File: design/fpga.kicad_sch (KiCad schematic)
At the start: 83 parts, among them J7 DEBUG_FPGA_GPIO, J8 DIGILENT_JTAG_HS2_01X06, SW1 RST, SW2 PROG, U13 XC7S15-FTGB196, U14 IS25LP064A-JKx

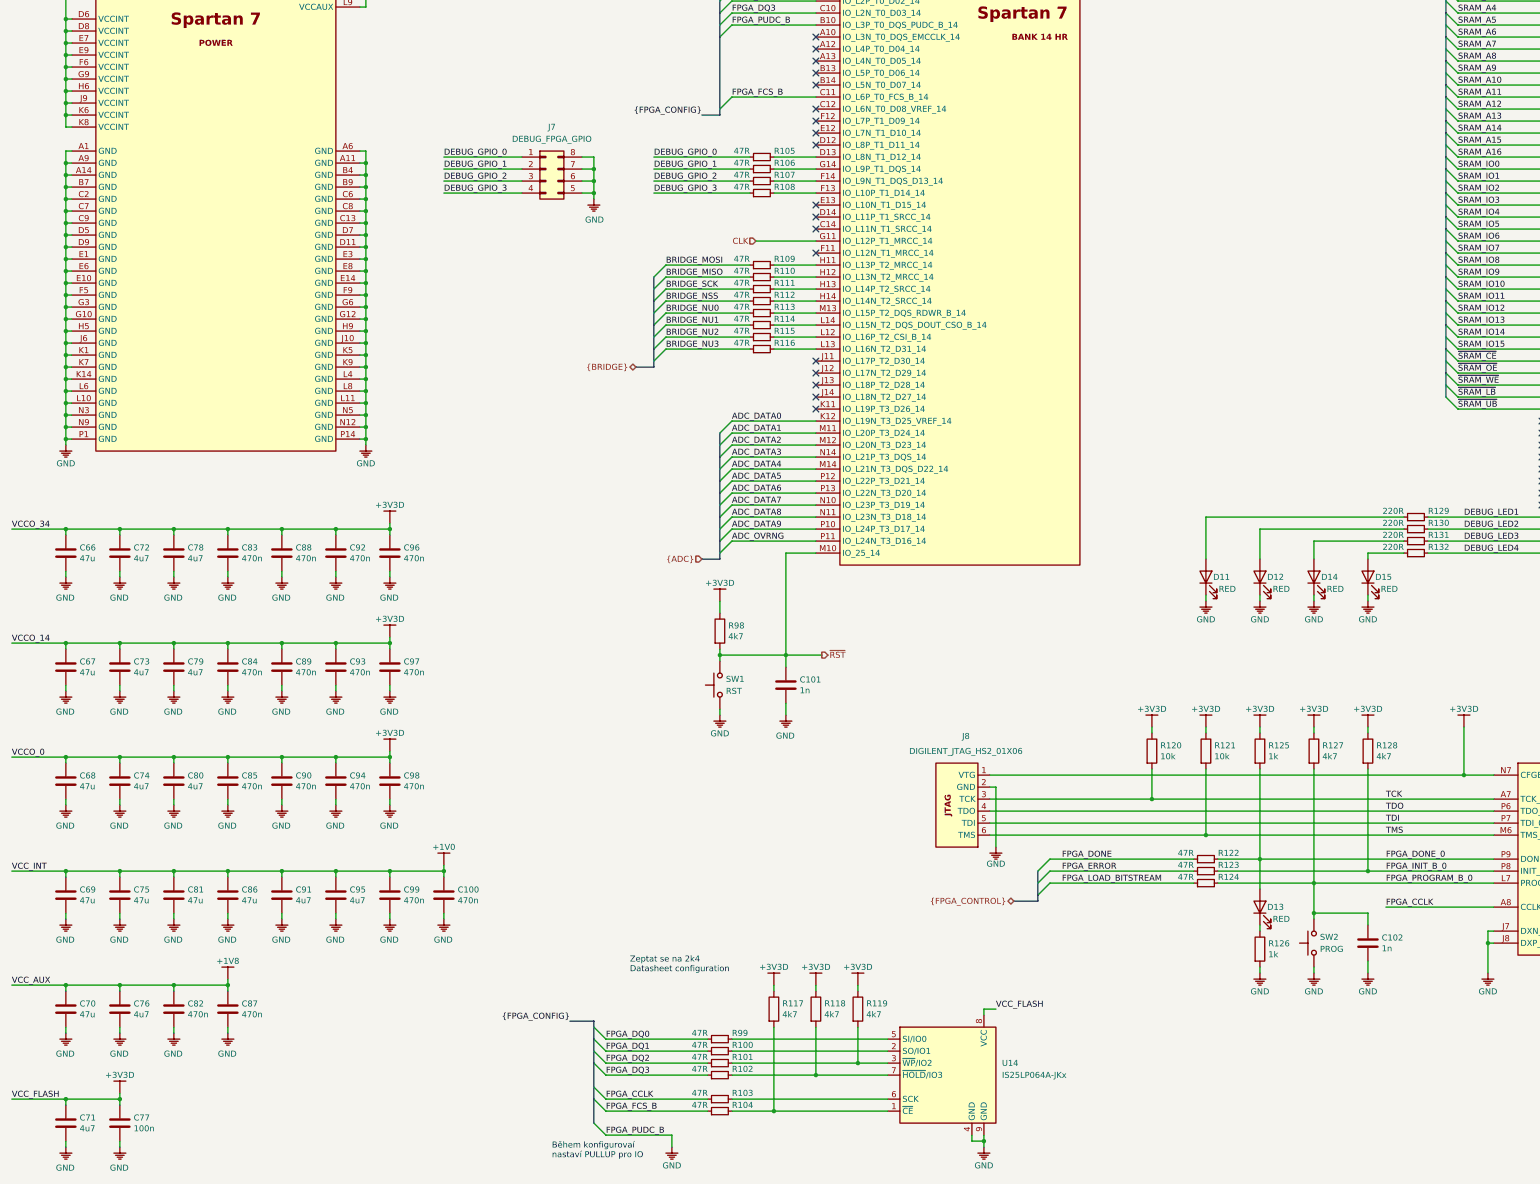
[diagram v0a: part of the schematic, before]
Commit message: Added ADC placement
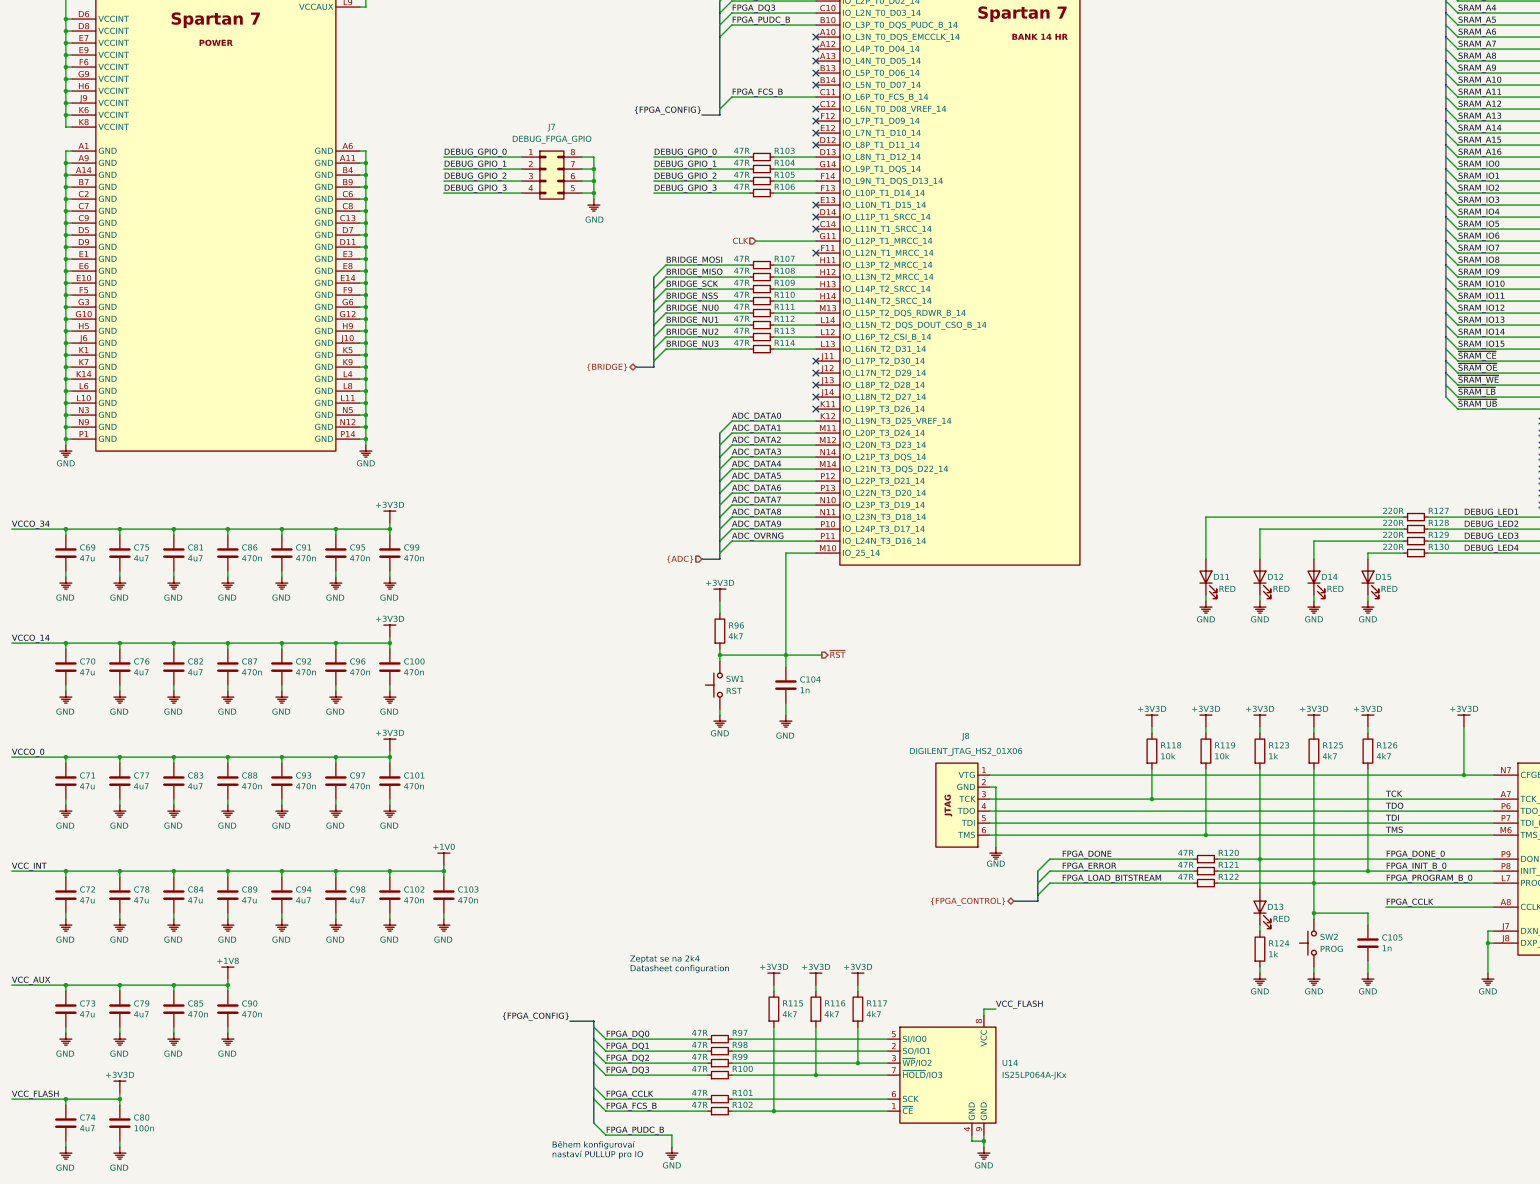
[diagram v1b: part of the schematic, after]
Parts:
- renumbered C97 to C100, C98 to C101, C99 to C102, C100 to C103, C101 to C104, C102 to C105, C66 to C69, C67 to C70, C68 to C71, C69 to C72, C70 to C73, C71 to C74, C72 to C75, C73 to C76, C74 to C77, C75 to C78, C76 to C79, C77 to C80, C78 to C81, C79 to C82, C80 to C83, C81 to C84, C82 to C85, C83 to C86, C84 to C87, C85 to C88, C86 to C89, C87 to C90, C88 to C91, C89 to C92, C90 to C93, C91 to C94, C92 to C95, C93 to C96, C94 to C97, C95 to C98, C96 to C99, R102 to R100, R103 to R101, R104 to R102, R105 to R103, R106 to R104, R107 to R105, R108 to R106, R109 to R107, R110 to R108, R111 to R109, R112 to R110, R113 to R111, R114 to R112, R115 to R113, R116 to R114, R117 to R115, R118 to R116, R119 to R117, R120 to R118, R121 to R119, R122 to R120, R123 to R121, R124 to R122, R125 to R123, R126 to R124, R127 to R125, R128 to R126, R129 to R127, R130 to R128, R131 to R129, R132 to R130, R98 to R96, R99 to R97, R100 to R98, R101 to R99

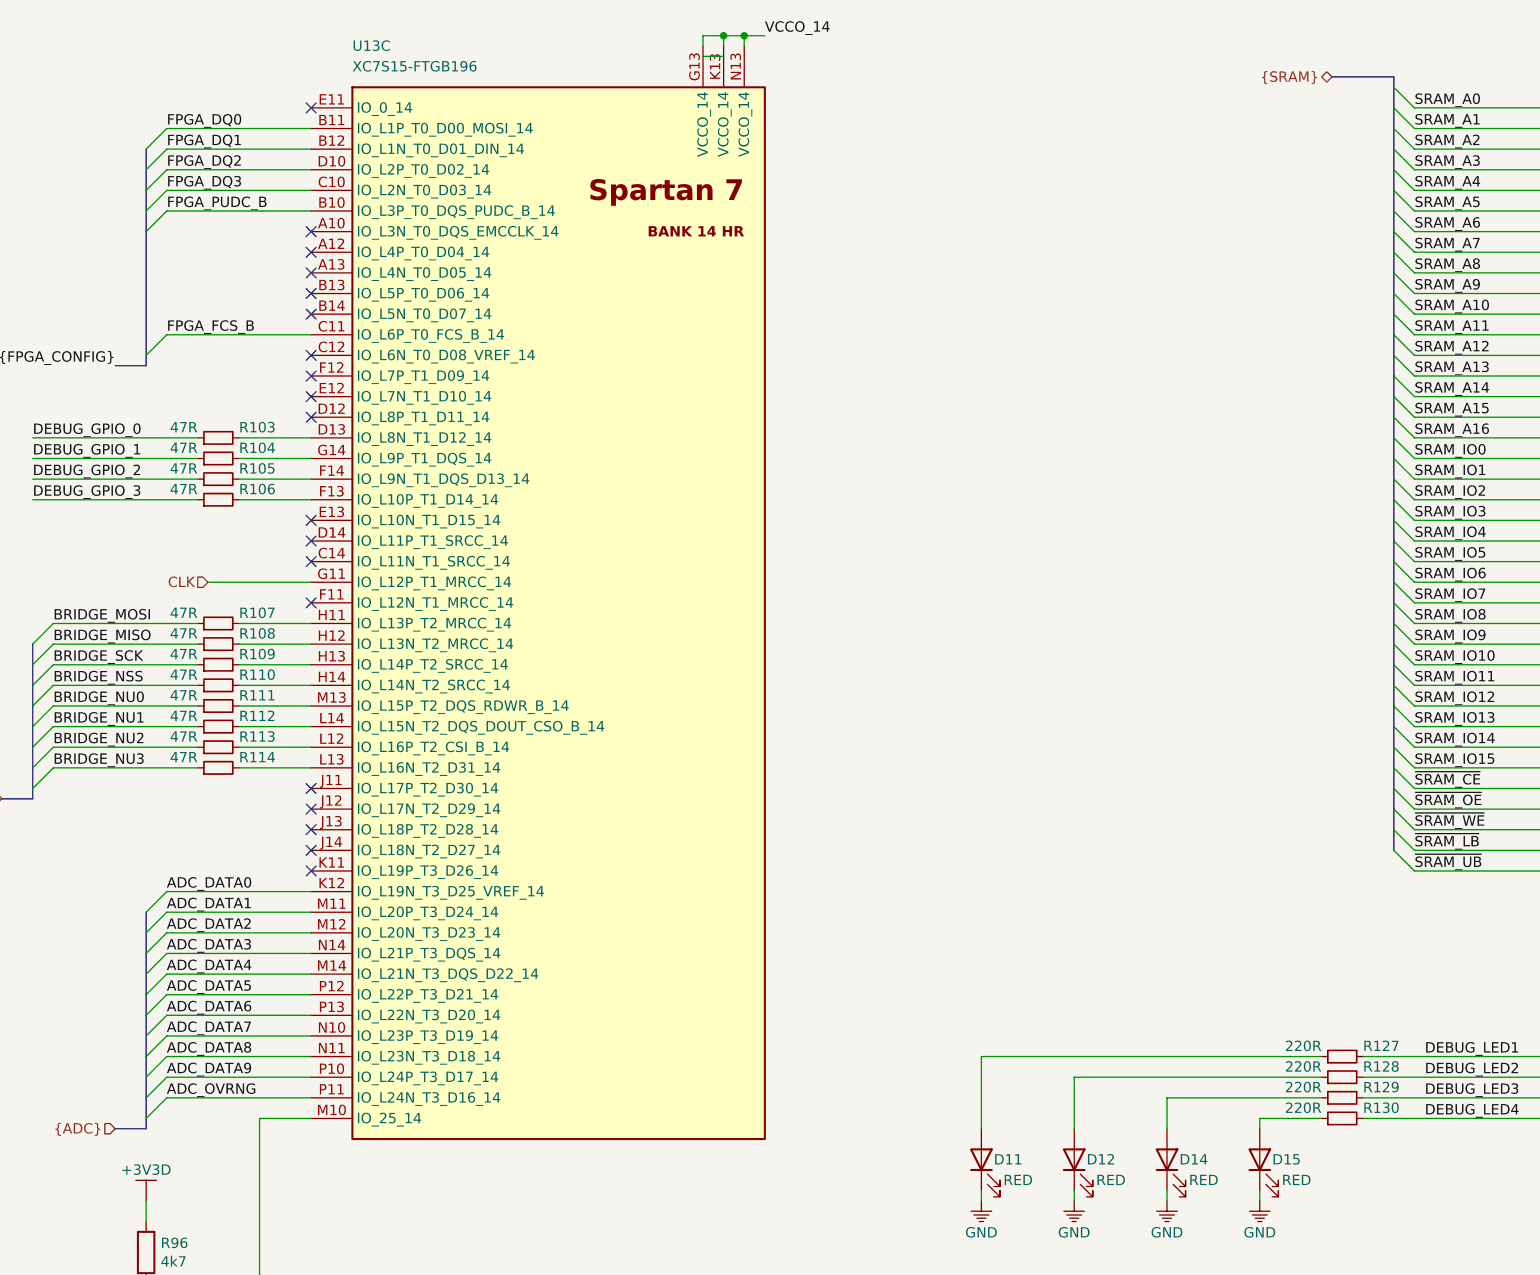
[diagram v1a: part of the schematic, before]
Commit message: Fixed LNA power
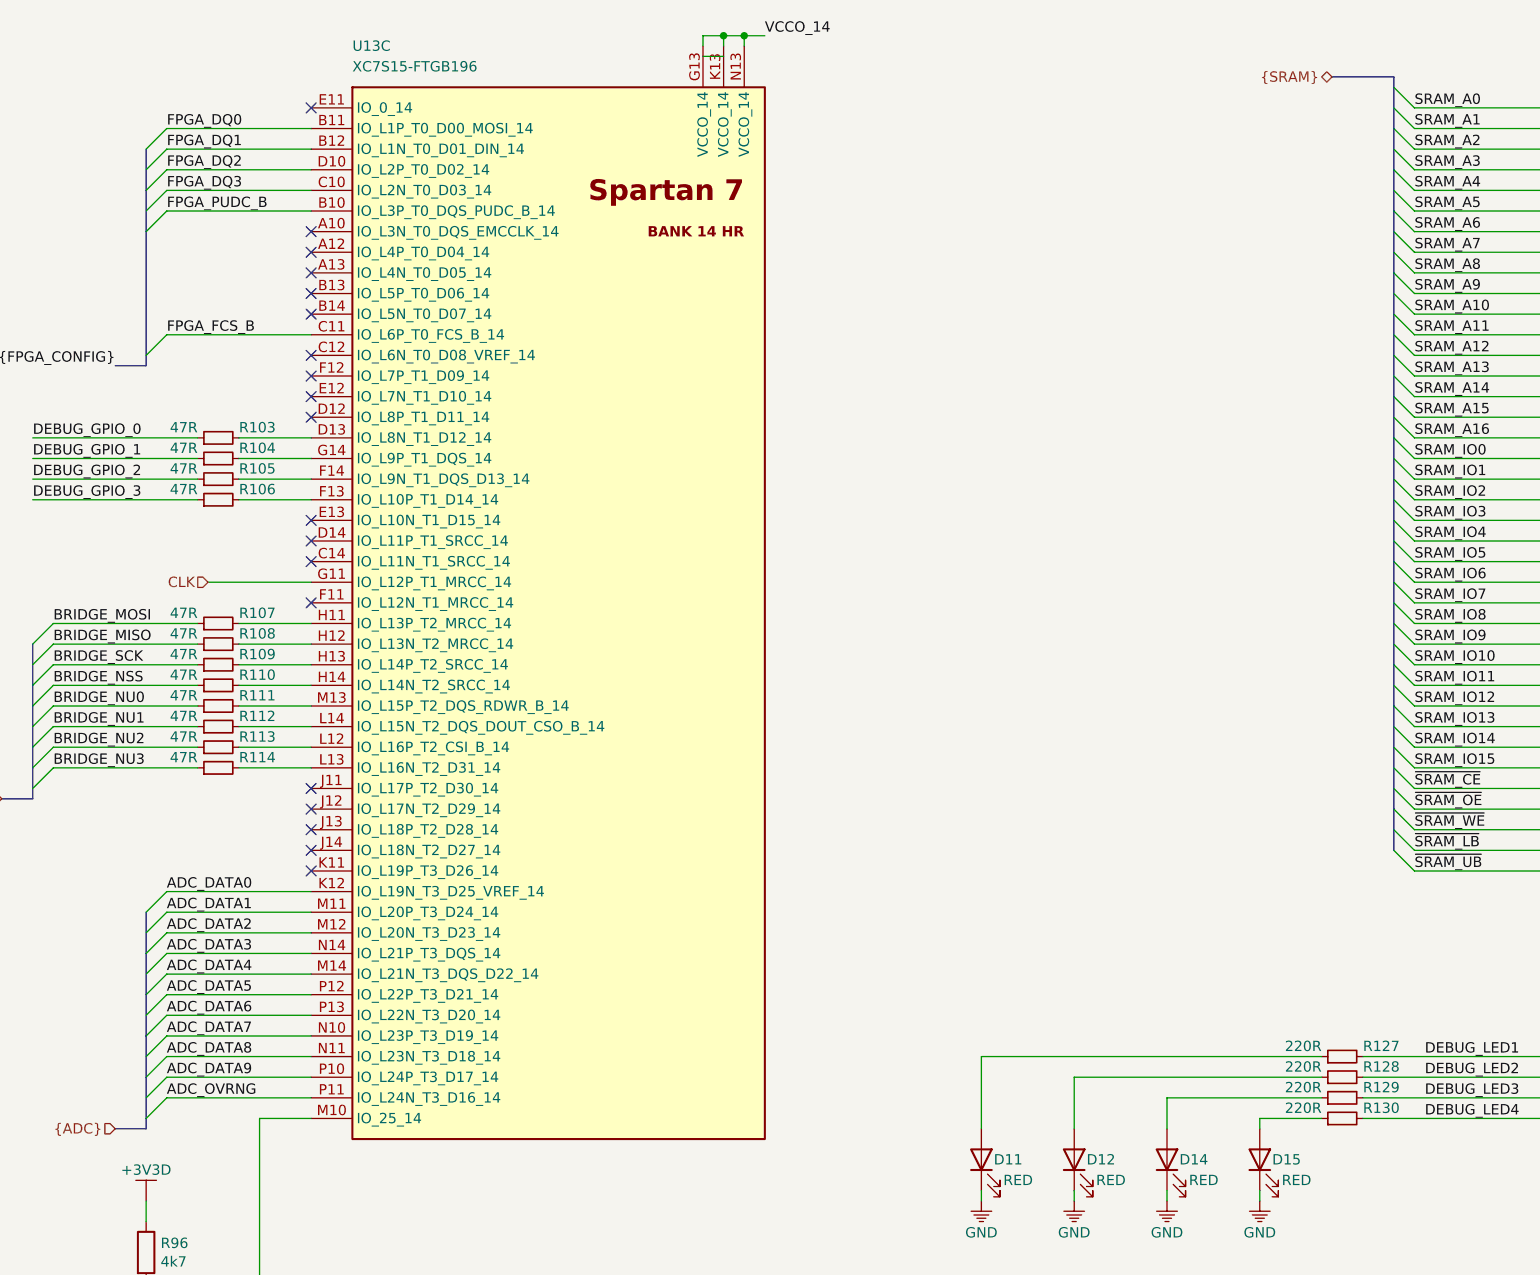
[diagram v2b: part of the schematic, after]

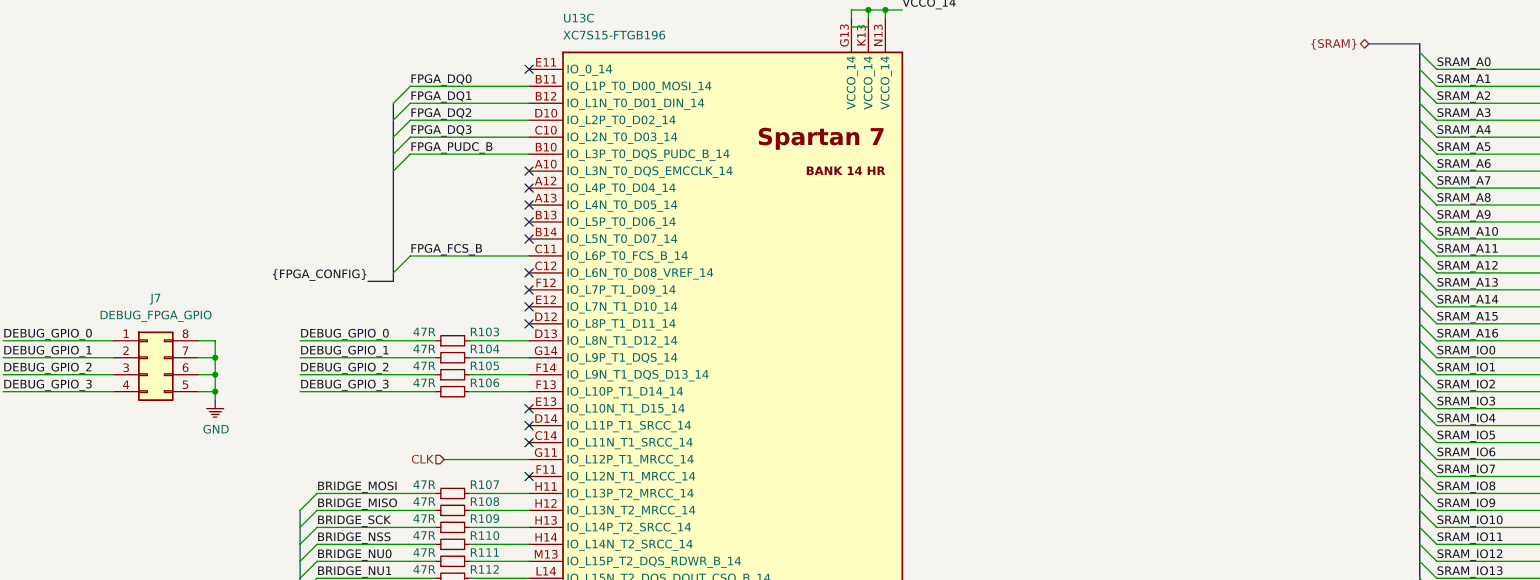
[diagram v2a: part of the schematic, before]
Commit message: Added basic FPGA placement
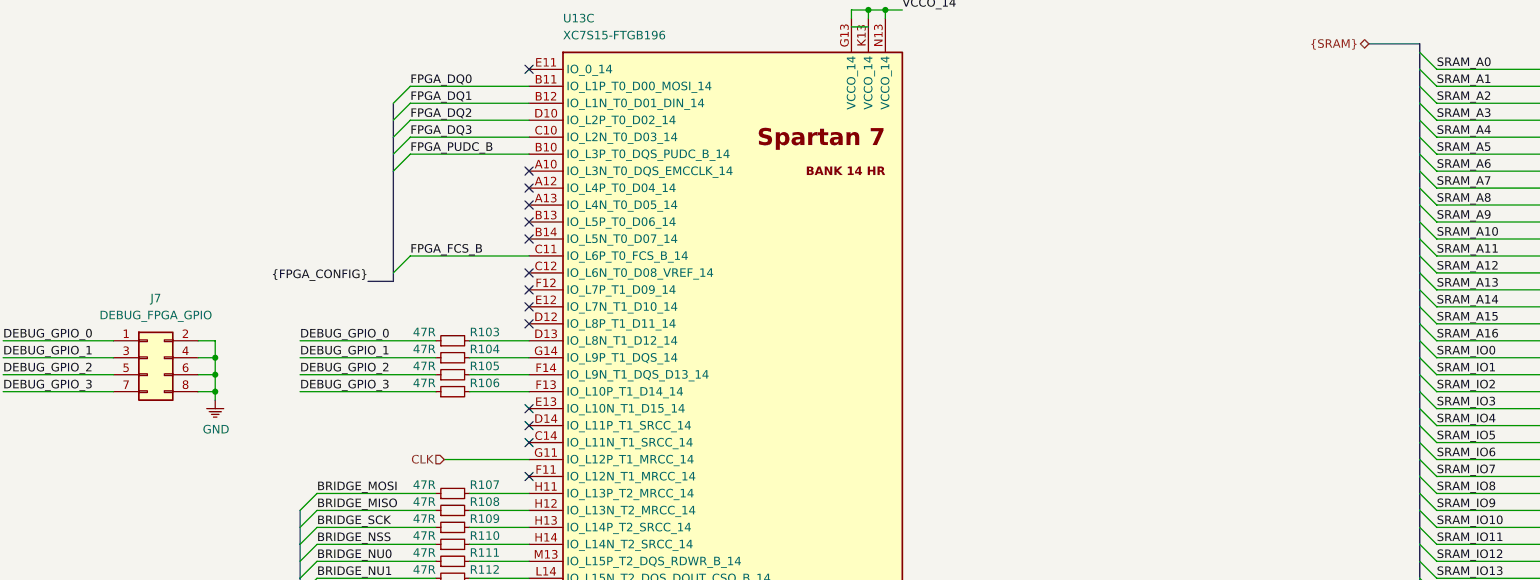
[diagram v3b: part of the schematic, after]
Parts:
- removed J7: DEBUG_FPGA_GPIO, Connector_PinHeader_2.54mm:PinHeader_2x04_P2.54mm_Vertical, symbol Connector_Generic:Conn_02x04_Counter_Clockwise
- added J7: DEBUG_FPGA_GPIO, Connector_PinHeader_2.54mm:PinHeader_2x04_P2.54mm_Vertical, symbol Connector_Generic:Conn_02x04_Odd_Even
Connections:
- net DEBUG_GPIO_0: now also J7.1 (Pin_1)
- net DEBUG_GPIO_1: now also J7.3 (Pin_3)
- net DEBUG_GPIO_2: now also J7.5 (Pin_5)
- net DEBUG_GPIO_3: now also J7.7 (Pin_7)
- net GND: now also J7.2 (Pin_2), J7.4 (Pin_4), J7.6 (Pin_6), J7.8 (Pin_8)
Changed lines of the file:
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@@
   (bus (pts (xy 318.77 22.86) (xy 318.77 27.94)))
   (bus (pts (xy 318.77 27.94) (xy 318.77 33.02)))
-  (bus (pts (xy 318.77 33.02) (xy 318.77 38.1)))
-  (bus (pts (xy 318.77 38.1) (xy 318.77 43.18)))
-  (bus (pts (xy 318.77 43.18) (xy 318.77 45.72)))
+  (bus (pts (xy 318.77 33.02) (xy 318.77 35.56)))
+  (bus (pts (xy 318.77 35.56) (xy 318.77 40.64)))
+  (bus (pts (xy 318.77 40.64) (xy 318.77 45.72)))
   (bus (pts (xy 318.77 45.72) (xy 318.77 50.8)))
   (bus (pts (xy 318.77 50.8) (xy 318.77 55.88)))
   (bus (pts (xy 318.77 55.88) (xy 318.77 60.96)))
-  (bus (pts (xy 318.77 60.96) (xy 318.77 66.04)))
-  (bus (pts (xy 318.77 66.04) (xy 318.77 71.12)))
-  (bus (pts (xy 318.77 71.12) (xy 318.77 76.2)))
-  (bus (pts (xy 318.77 76.2) (xy 318.77 81.28)))
-  (bus (pts (xy 318.77 81.28) (xy 318.77 83.82)))
+  (bus (pts (xy 318.77 60.96) (xy 318.77 63.5)))
+  (bus (pts (xy 318.77 63.5) (xy 318.77 68.58)))
+  (bus (pts (xy 318.77 68.58) (xy 318.77 73.66)))
+  (bus (pts (xy 318.77 73.66) (xy 318.77 78.74)))
+  (bus (pts (xy 318.77 78.74) (xy 318.77 83.82)))
   (bus (pts (xy 318.77 83.82) (xy 318.77 88.9)))
   (bus (pts (xy 318.77 88.9) (xy 318.77 93.98)))
@@
     )
   )
-  (symbol (lib_id "Connector_Generic:Conn_02x04_Counter_Clockwise") (at 128.27 68.58 0) (unit 1)
+  (symbol (lib_id "Connector_Generic:Conn_02x04_Odd_Even") (at 128.27 68.58 0) (unit 1)
     (property "Reference" "J7" (id 0) (at 129.54 59.69 0))
     (property "Value" "DEBUG_FPGA_GPIO" (id 1) (at 129.54 62.23 0))
